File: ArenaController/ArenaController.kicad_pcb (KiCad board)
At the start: 2 copper layers, 80 x 90 mm, 29 parts, among them J1 RJ45, J2 RJ45, J4 RJ45, J5 RJ45, J6 RJ45, J9 Barrel_Jack_MountingPin, Q1 FS3400, Q2 FS3400, Q3 FS3400, Q4 FS3400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

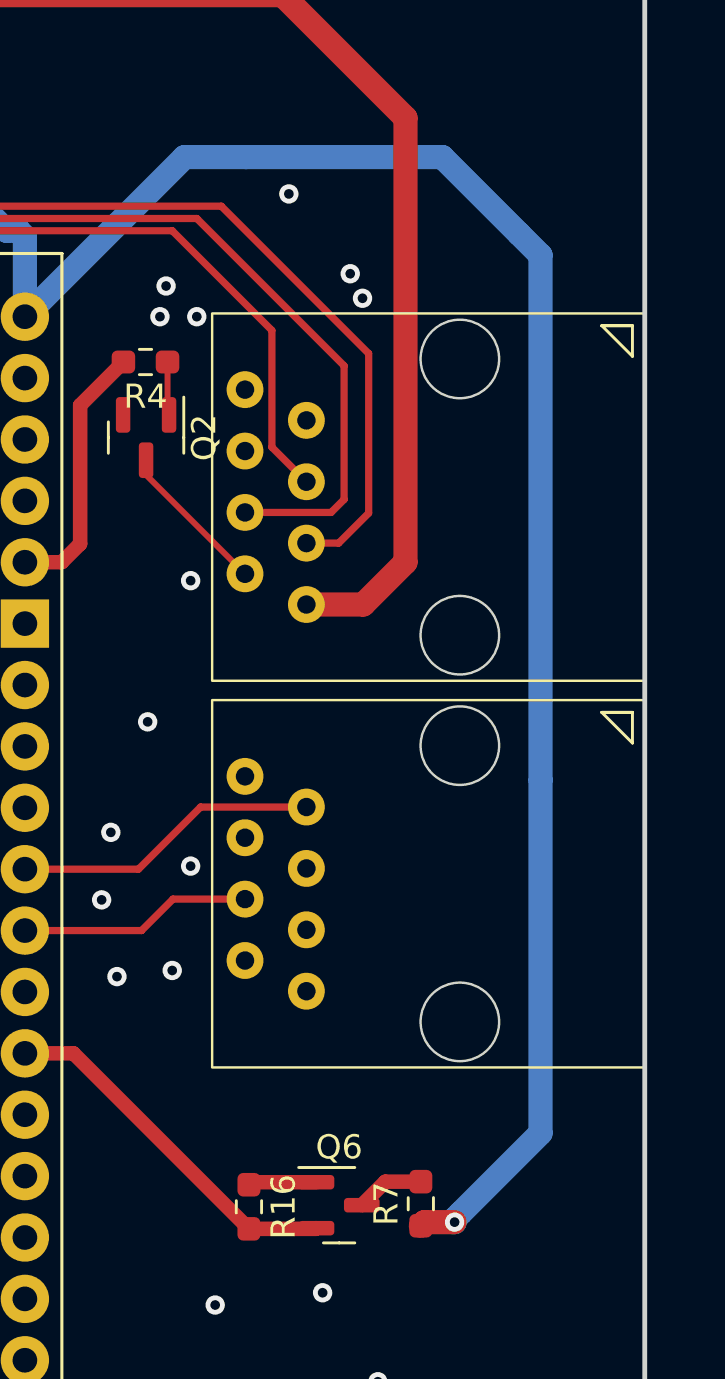
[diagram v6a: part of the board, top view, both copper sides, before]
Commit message: Swap to a footprint with the correctly named pin in our project repo.  Yay!
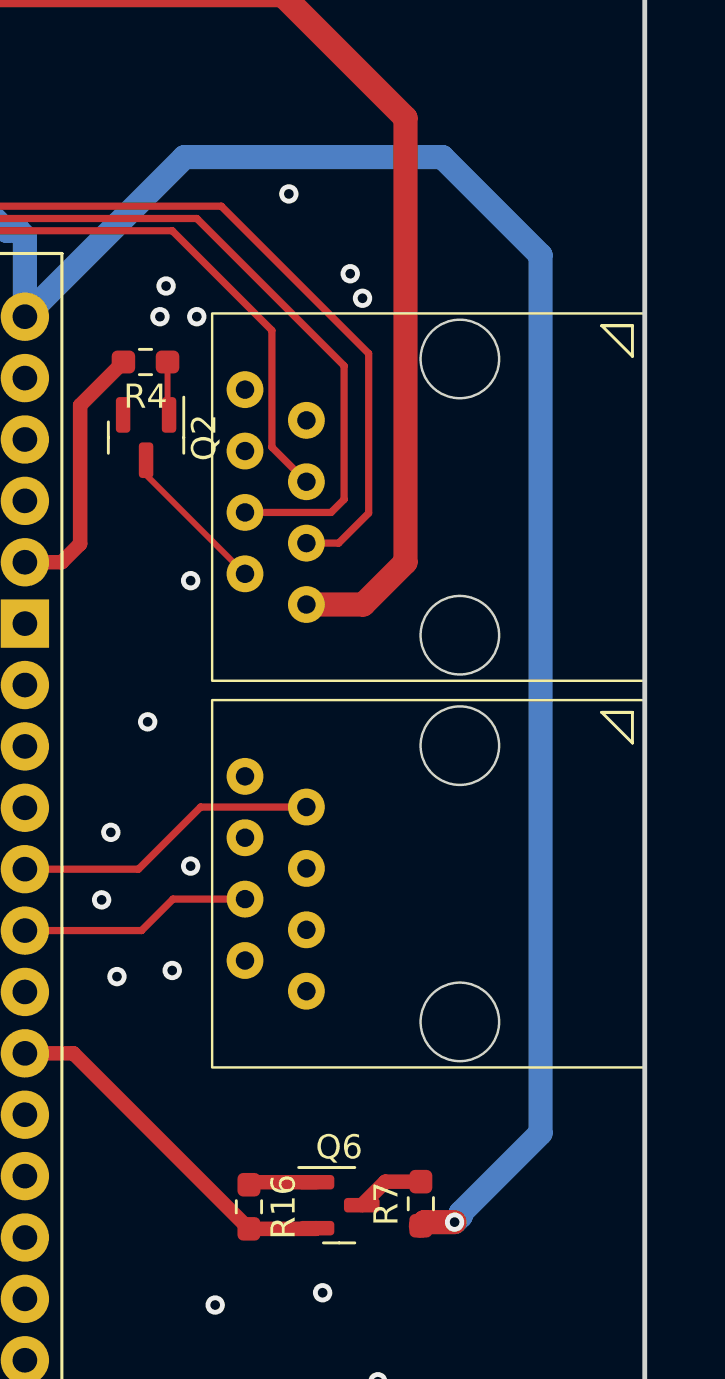
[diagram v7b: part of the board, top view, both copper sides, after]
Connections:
- J9 pad 3: (no net) -> unconnected-(J9-MountPin-Pad3)
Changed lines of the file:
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@@
   (net 72 "unconnected-(U3-GPIO18{slash}V_SPI_CLK{slash}SCK-Pad11)")
   (net 73 "unconnected-(U3-RTC_GPIO5{slash}ADC1_7{slash}GPIO35-Pad25)")
+  (net 74 "unconnected-(J9-MountPin-Pad3)")
   (footprint "Resistor_SMD:R_0603_1608Metric_Pad0.98x0.95mm_HandSolder" (layer "F.Cu")
     (at 158.623 108.966 -90)
@@
     (pad "2" thru_hole roundrect (at -6 0 270) (size 3 3.5) (drill oval 1 3) (layers "*.Cu" "*.Mask") (roundrect_rratio 0.25)
       (net 6 "GND") (pintype "passive"))
-    (pad "3" thru_hole roundrect (at -3 4.7 270) (size 3.5 3.5) (drill oval 3 1) (layers "*.Cu" "*.Mask") (roundrect_rratio 0.25))
+    (pad "3" thru_hole roundrect (at -3 4.7 270) (size 3.5 3.5) (drill oval 3 1) (layers "*.Cu" "*.Mask") (roundrect_rratio 0.25)
+      (net 74 "unconnected-(J9-MountPin-Pad3)") (pinfunction "MountPin") (pintype "passive"))
     (model "${KICAD6_3DMODEL_DIR}/Connector_BarrelJack.3dshapes/BarrelJack_Horizontal.wrl"
       (offset (xyz 0 0 0))
@@
   (segment (start 156.622 92.425) (end 154.051 94.996) (width 0.3) (layer "F.Cu") (net 16))
   (segment (start 154.051 94.996) (end 149.352 94.996) (width 0.3) (layer "F.Cu") (net 16))
-  (segment (start 167.132 109.601) (end 165.8855 109.601) (width 1) (layer "F.Cu") (net 33))
   (segment (start 133.10875 55.13075) (end 132.08 56.1595) (width 0.6) (layer "F.Cu") (net 33))
-  (segment (start 165.8855 109.601) (end 165.735 109.7515) (width 1) (layer "F.Cu") (net 33))
   (segment (start 134.62 53.6195) (end 133.10875 55.13075) (width 0.6) (layer "F.Cu") (net 33))
   (segment (start 126.817084 56.8595) (end 131.38 56.8595) (width 0.6) (layer "F.Cu") (net 33))
@@
   (segment (start 133.10875 55.13075) (end 135.14075 55.13075) (width 0.6) (layer "F.Cu") (net 33))
   (segment (start 135.14075 55.13075) (end 136.398 56.388) (width 0.6) (layer "F.Cu") (net 33))
+  (segment (start 167.132 109.601) (end 165.8855 109.601) (width 1) (layer "F.Cu") (net 33))
+  (segment (start 165.8855 109.601) (end 165.735 109.7515) (width 1) (layer "F.Cu") (net 33))
   (segment (start 134.62 52.3215) (end 134.62 53.6195) (width 0.6) (layer "F.Cu") (net 33))
   (segment (start 125.984 56.026416) (end 126.817084 56.8595) (width 0.6) (layer "F.Cu") (net 33))
   (via (at 167.132 109.601) (size 0.8) (drill 0.4) (layers "F.Cu" "B.Cu") (net 33))
   (via (at 136.398 56.388) (size 0.8) (drill 0.4) (layers "F.Cu" "B.Cu") (net 33))
-  (segment (start 169.799 68.707) (end 170.688 69.596) (width 1) (layer "B.Cu") (net 33))
-  (segment (start 167.386 109.22) (end 167.132 109.474) (width 1) (layer "B.Cu") (net 33))
+  (segment (start 167.386 109.22) (end 167.386 109.347) (width 1) (layer "B.Cu") (net 33))
+  (segment (start 155.956 65.532) (end 166.624 65.532) (width 1) (layer "B.Cu") (net 33))
+  (segment (start 149.352 72.136) (end 155.956 65.532) (width 1) (layer "B.Cu") (net 33))
   (segment (start 149.352 68.834) (end 149.098 68.58) (width 1) (layer "B.Cu") (net 33))
   (segment (start 149.352 68.834) (end 149.352 72.136) (width 1) (layer "B.Cu") (net 33))
-  (segment (start 166.624 65.532) (end 169.799 68.707) (width 1) (layer "B.Cu") (net 33))
-  (segment (start 149.352 72.136) (end 155.956 65.532) (width 1) (layer "B.Cu") (net 33))
-  (segment (start 170.688 91.313) (end 170.688 105.918) (width 1) (layer "B.Cu") (net 33))
-  (segment (start 170.688 105.918) (end 167.386 109.22) (width 1) (layer "B.Cu") (net 33))
-  (segment (start 170.688 69.596) (end 170.688 91.313) (width 1) (layer "B.Cu") (net 33))
+  (segment (start 167.386 109.347) (end 167.132 109.601) (width 1) (layer "B.Cu") (net 33))
+  (segment (start 170.688 69.596) (end 170.688 105.918) (width 1) (layer "B.Cu") (net 33))
   (segment (start 149.098 68.58) (end 148.59 68.58) (width 1) (layer "B.Cu") (net 33))
-  (segment (start 167.132 109.474) (end 167.132 109.601) (width 1) (layer "B.Cu") (net 33))
-  (segment (start 158.496 65.532) (end 166.624 65.532) (width 1) (layer "B.Cu") (net 33))
-  (segment (start 167.132 109.601) (end 167.005 109.601) (width 1) (layer "B.Cu") (net 33))
-  (segment (start 155.956 65.532) (end 158.496 65.532) (width 1) (layer "B.Cu") (net 33))
+  (segment (start 166.624 65.532) (end 170.688 69.596) (width 1) (layer "B.Cu") (net 33))
+  (segment (start 170.688 105.918) (end 167.386 109.22) (width 1) (layer "B.Cu") (net 33))
   (segment (start 148.59 68.58) (end 136.398 56.388) (width 1) (layer "B.Cu") (net 33))
   (segment (start 114.8865 73.0785) (end 111.54 76.425) (width 0.3) (layer "F.Cu") (net 35))

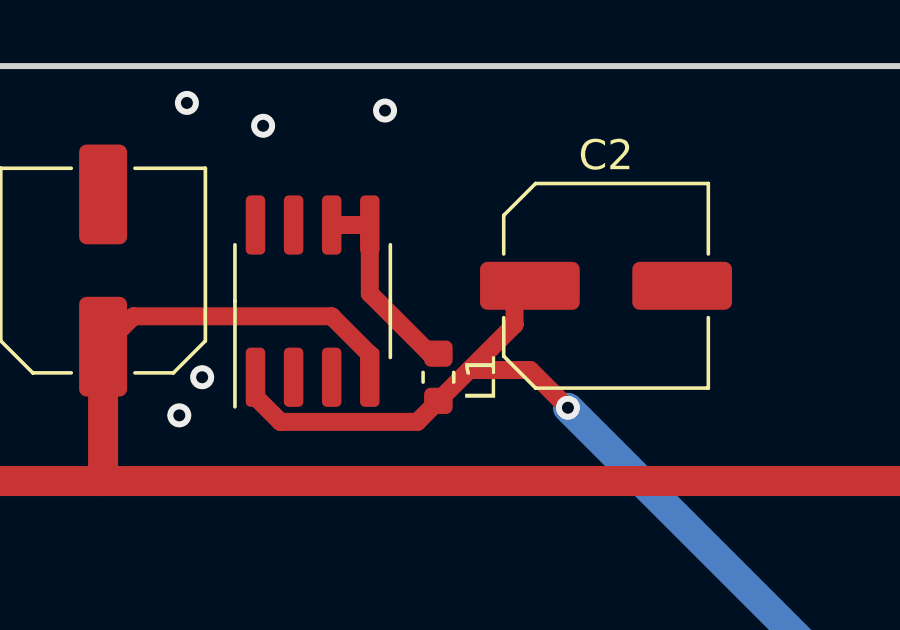
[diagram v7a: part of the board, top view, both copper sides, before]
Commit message: Added initial teamsign and update symbol mistakes, mostly.
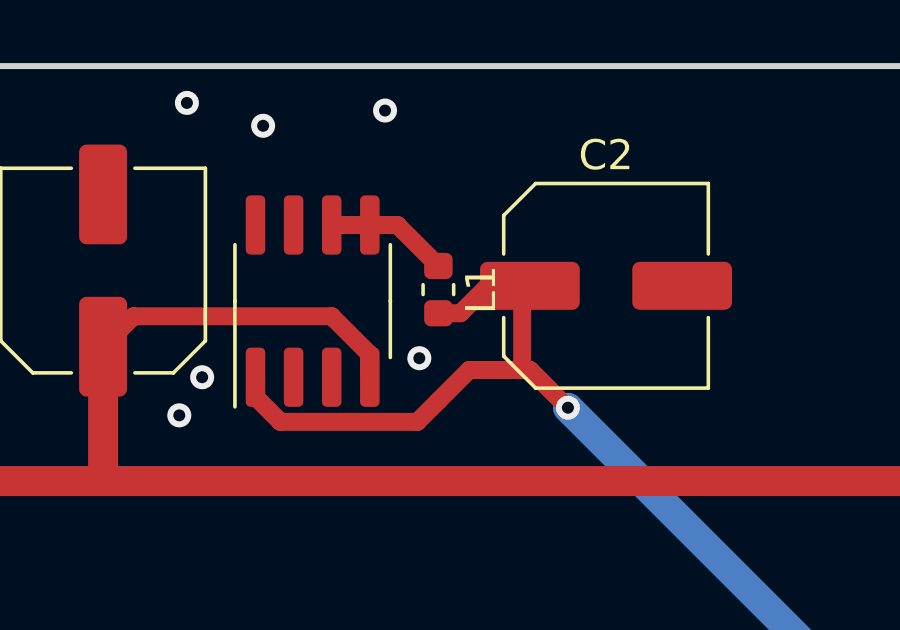
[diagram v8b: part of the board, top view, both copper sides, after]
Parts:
- moved L1 2.92 mm to (132.1, 52.5)
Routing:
- net +5V: track 105.5 -> 108.4 mm
- net Net-(L1-Pad1): track 6.67 -> 4.12 mm
- net GND: vias 31 -> 32
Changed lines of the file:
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@@
   )
   (footprint "Inductor_SMD:L_0603_1608Metric" (layer "F.Cu")
-    (at 132.08 55.372 -90)
+    (at 132.08 52.451 -90)
     (descr "Inductor SMD 0603 (1608 Metric), square (rectangular) end terminal, IPC_7351 nominal, (Body size source: http://www.tortai-tech.com/upload/download/2011102023233369053.pdf), generated with kicad-footprint-generator")
     (tags "inductor")
@@
   (via (at 155.194 70.866) (size 0.8) (drill 0.4) (layers "F.Cu" "B.Cu") (free) (net 6))
   (via (at 157.226 113.03) (size 0.8) (drill 0.4) (layers "F.Cu" "B.Cu") (free) (net 6))
+  (via (at 131.445 54.737) (size 0.8) (drill 0.4) (layers "F.Cu" "B.Cu") (free) (net 6))
   (segment (start 111.54 111.765) (end 113.787 111.765) (width 0.25) (layer "B.Cu") (net 9))
   (segment (start 113.787 111.765) (end 120.396 105.156) (width 0.25) (layer "B.Cu") (net 9))
@@
   (segment (start 154.051 94.996) (end 149.352 94.996) (width 0.3) (layer "F.Cu") (net 16))
   (segment (start 133.10875 55.13075) (end 132.08 56.1595) (width 0.6) (layer "F.Cu") (net 33))
-  (segment (start 134.62 53.6195) (end 133.10875 55.13075) (width 0.6) (layer "F.Cu") (net 33))
+  (segment (start 135.1305 52.324) (end 134.874 52.5805) (width 0.6) (layer "F.Cu") (net 33))
+  (segment (start 132.8165 53.2385) (end 133.731 52.324) (width 0.6) (layer "F.Cu") (net 33))
+  (segment (start 134.874 52.5805) (end 134.874 55.13075) (width 0.6) (layer "F.Cu") (net 33))
   (segment (start 126.817084 56.8595) (end 131.38 56.8595) (width 0.6) (layer "F.Cu") (net 33))
+  (segment (start 133.731 52.324) (end 135.1305 52.324) (width 0.6) (layer "F.Cu") (net 33))
   (segment (start 131.38 56.8595) (end 132.08 56.1595) (width 0.6) (layer "F.Cu") (net 33))
-  (segment (start 133.10875 55.13075) (end 135.14075 55.13075) (width 0.6) (layer "F.Cu") (net 33))
   (segment (start 135.14075 55.13075) (end 136.398 56.388) (width 0.6) (layer "F.Cu") (net 33))
+  (segment (start 133.10875 55.13075) (end 134.874 55.13075) (width 0.6) (layer "F.Cu") (net 33))
+  (segment (start 132.08 53.2385) (end 132.8165 53.2385) (width 0.6) (layer "F.Cu") (net 33))
   (segment (start 167.132 109.601) (end 165.8855 109.601) (width 1) (layer "F.Cu") (net 33))
   (segment (start 165.8855 109.601) (end 165.735 109.7515) (width 1) (layer "F.Cu") (net 33))
-  (segment (start 134.62 52.3215) (end 134.62 53.6195) (width 0.6) (layer "F.Cu") (net 33))
+  (segment (start 134.874 55.13075) (end 135.14075 55.13075) (width 0.6) (layer "F.Cu") (net 33))
   (segment (start 125.984 56.026416) (end 126.817084 56.8595) (width 0.6) (layer "F.Cu") (net 33))
   (via (at 167.132 109.601) (size 0.8) (drill 0.4) (layers "F.Cu" "B.Cu") (net 33))
@@
   (segment (start 158.7265 107.95) (end 158.623 108.0535) (width 0.6) (layer "F.Cu") (net 51))
   (segment (start 161.417 107.95) (end 158.7265 107.95) (width 0.6) (layer "F.Cu") (net 51))
-  (segment (start 132.08 54.5845) (end 131.8005 54.5845) (width 0.6) (layer "F.Cu") (net 70))
-  (segment (start 129.794 52.578) (end 129.794 50.297) (width 0.6) (layer "F.Cu") (net 70))
+  (segment (start 129.794 50.297) (end 130.7135 50.297) (width 0.6) (layer "F.Cu") (net 70))
   (segment (start 129.794 50.297) (end 128.524 50.297) (width 0.6) (layer "F.Cu") (net 70))
-  (segment (start 131.8005 54.5845) (end 129.794 52.578) (width 0.6) (layer "F.Cu") (net 70))
+  (segment (start 130.7135 50.297) (end 132.08 51.6635) (width 0.6) (layer "F.Cu") (net 70))
   (zone (net 6) (net_name "GND") (layers "F&B.Cu") (hatch edge 0.5)
     (connect_pads (clearance 0.508))
